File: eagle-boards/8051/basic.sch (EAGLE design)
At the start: 12 parts, among them IC1 AT89S51-24P, Q1 12M

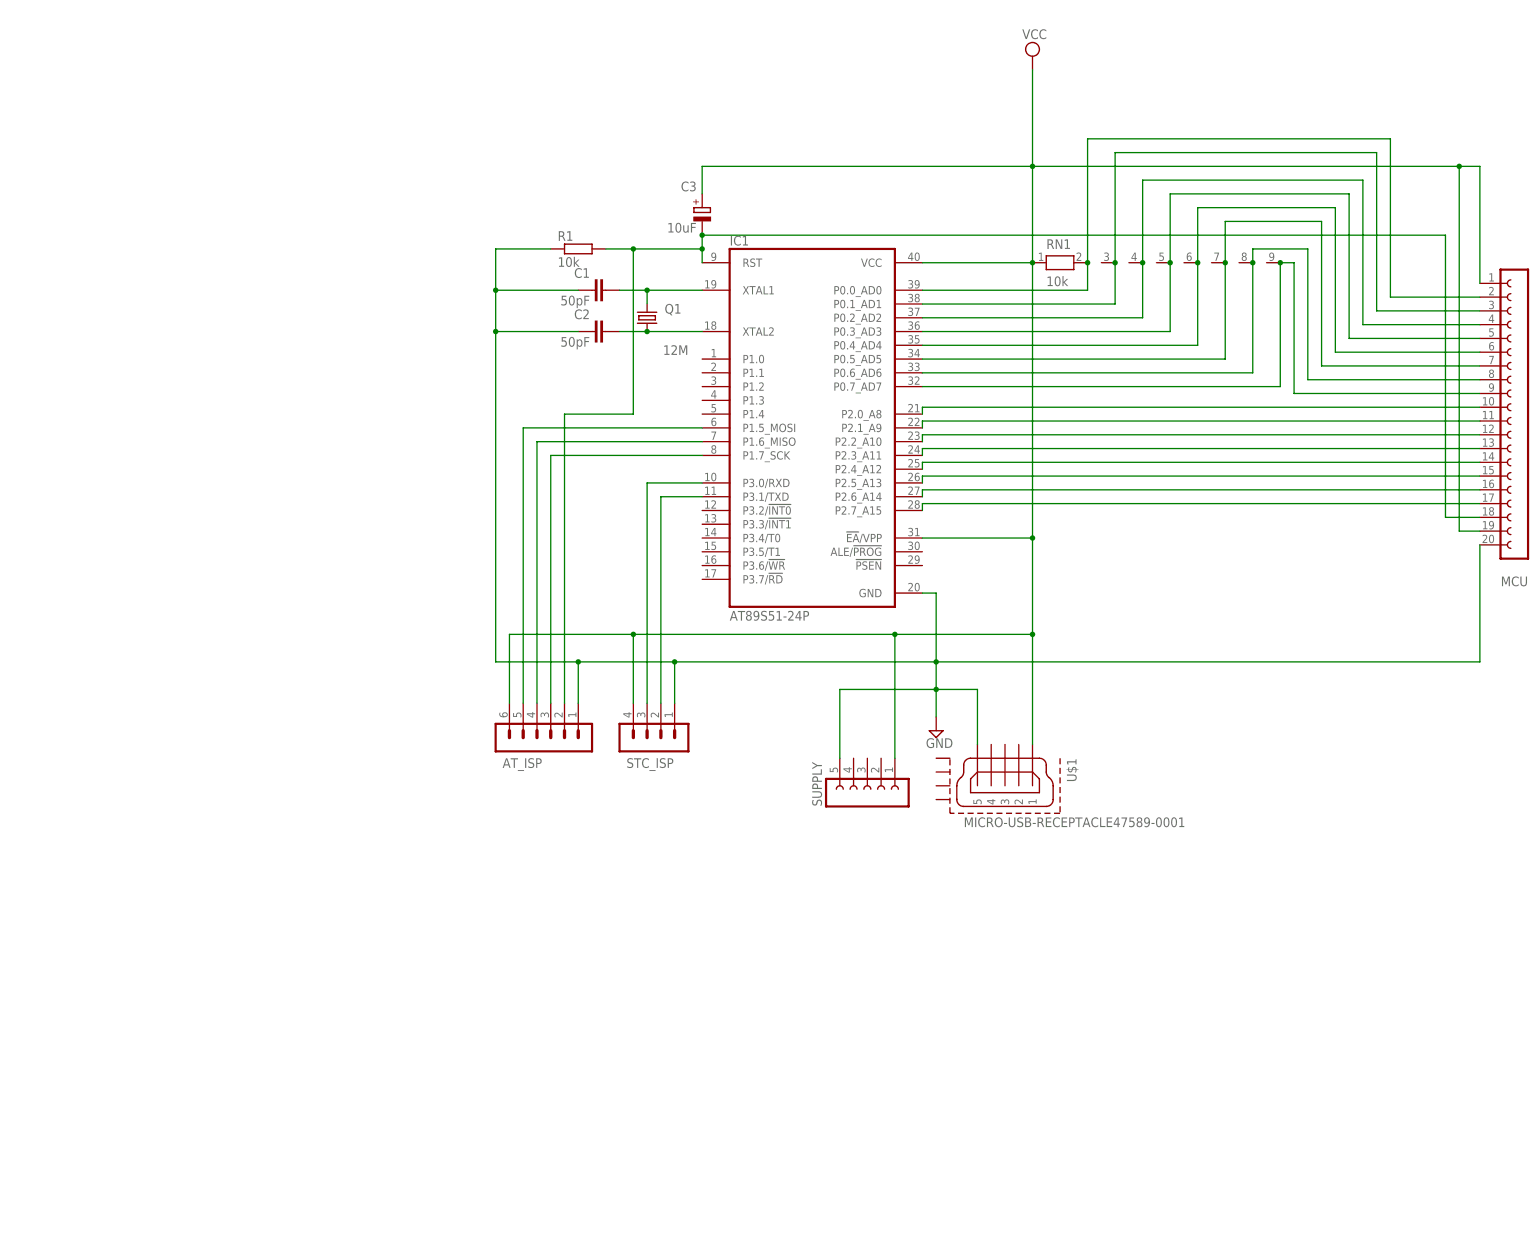
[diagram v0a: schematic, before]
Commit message: New revision for the STC89C52 controller board.
Include (optional) CP2104 USB-to-UART adapter to make it easier to program the board in-system.

Include a latching pushbutton for power, which is also needed to work correctly for in-system programming.
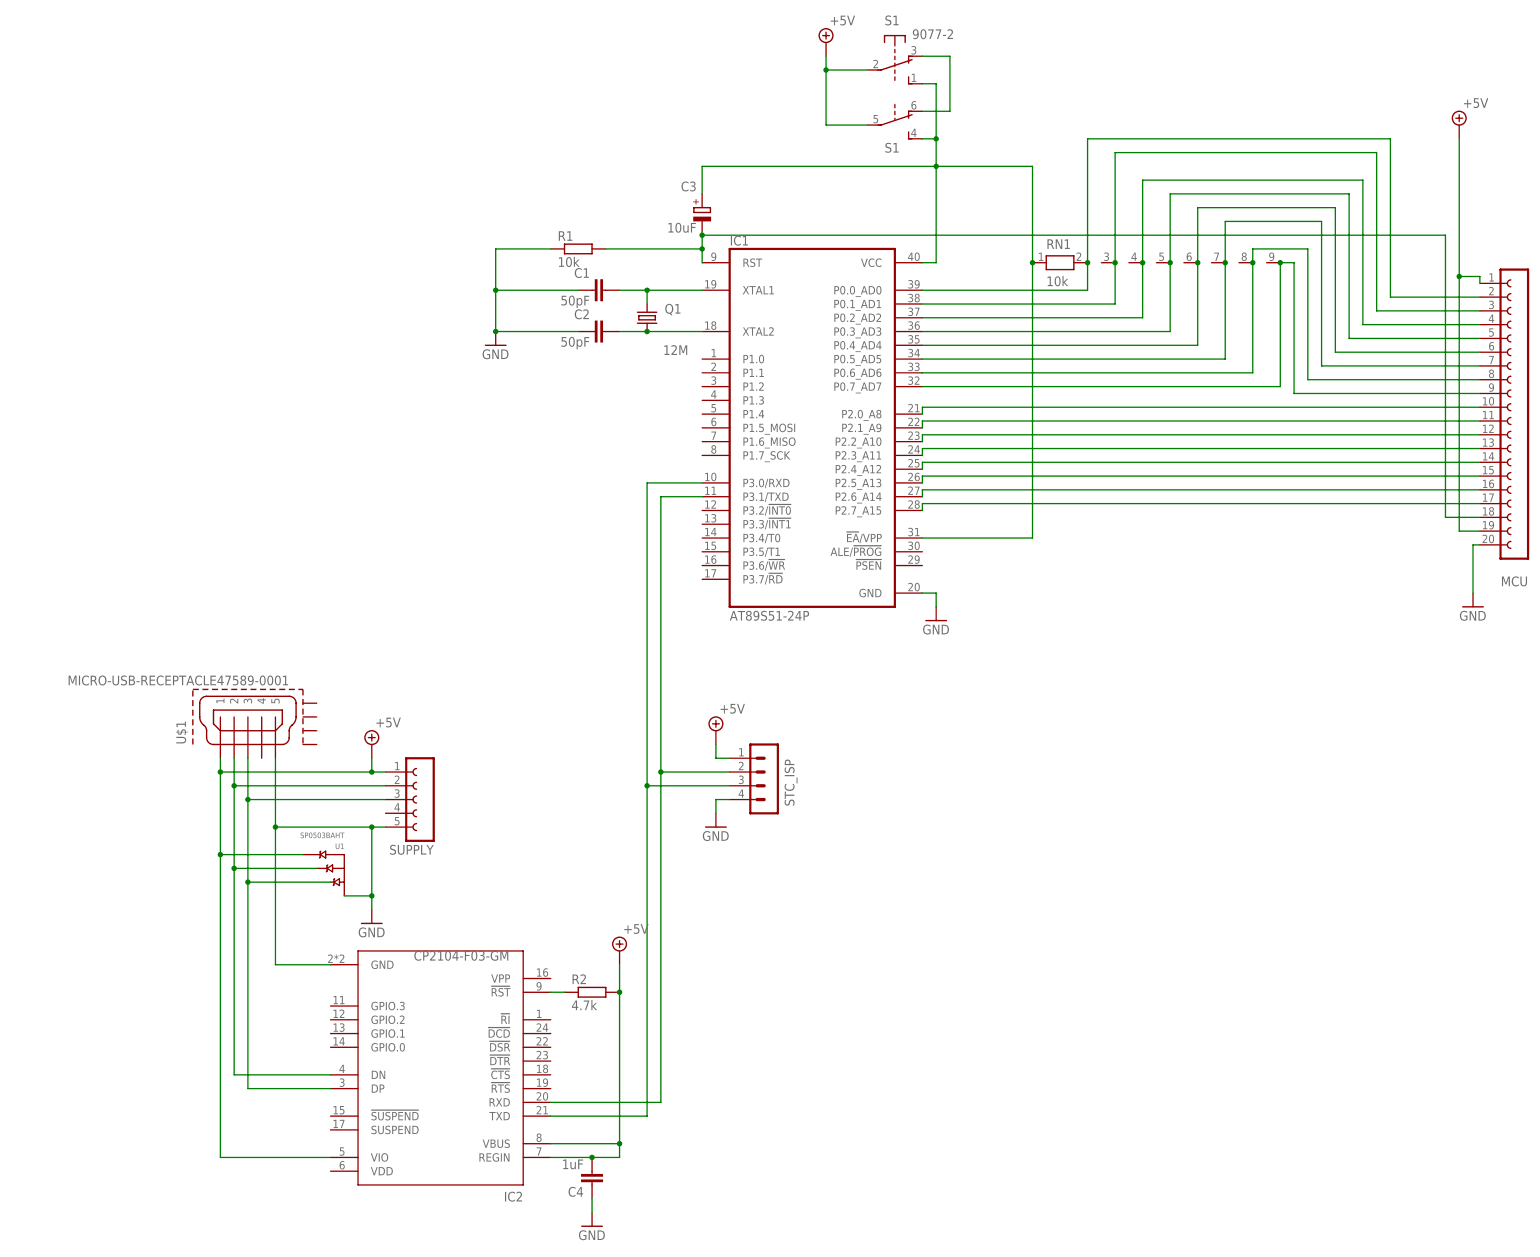
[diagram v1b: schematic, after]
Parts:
- removed AT_ISP: (no value), con-lstb:MA06-1
- added C4: 1uF, rcl:C-EU025-024X044
- added IC2: CP2104-F03-GM, CP2104:CP2104-F03-GM
- added R2: 4.7k, rcl:R-EU_0207/10
- added S1: 9077-2, switch-misc:9077-2
- added U1: SP0503BAHT, SP0503BAHT:SP0503BAHT
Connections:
- removed net N$49: AT_ISP.3, IC1.P1.7_SCK
- removed net N$50: AT_ISP.4, IC1.P1.6_MISO
- removed net N$51: AT_ISP.5, IC1.P1.5_MOSI
- removed net VCC: AT_ISP.6, C3.+, IC1.!EA!/VPP, IC1.VCC, MCU.1, MCU.19, RN1.1, STC_ISP.4, SUPPLY.1, U$1.1
- new net +5V: C4.2, IC2.REGIN, IC2.VBUS, IC2.VIO, MCU.1, MCU.19, R2.2, S11.P, S12.P, STC_ISP.1, SUPPLY.1, U$1.1, U1.C
- new net N$1: IC2.DN, SUPPLY.2, U$1.2, U1.B
- new net N$20: IC2.DP, SUPPLY.3, U$1.3, U1.A
- new net N$23: S11.O, S12.O
- new net N$24: IC2.!RST!, R2.1
- new net N$27: C3.+, IC1.!EA!/VPP, IC1.VCC, RN1.1, S11.S, S12.S
- net GND: now also C4.1, IC2.GND, STC_ISP.4, U1.GND; no longer AT_ISP.1, STC_ISP.1
- net N$18: now also IC2.TXD
- net N$5: no longer AT_ISP.2
- net N$52: now also IC2.RXD
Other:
- moved on the sheet: STC_ISP, SUPPLY, U$1

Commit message: Update components and layout for 8051 board.
Replace the microUSB connector to be the same Amphenol part as used in the ATmega board.

Replace the single electrolytic with a ceramic capacitor, and match the footprint between that and the CP2104 one.
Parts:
- C3: device rcl:CPOL-EUE2.5-6 -> capacitor-wima:C2.5/2
- C4: device rcl:C-EU025-024X044 -> capacitor-wima:C2.5/2
- U$1: value MICRO-USB-RECEPTACLE47589-0001 -> 10103594-0001LF; device con-molex-usb:MICRO-USB-RECEPTACLE47589-0001 -> 10103594-0001LF:10103594-0001LF
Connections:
- net N$27: now also C3.1; no longer C3.+
- net N$5: now also C3.2; no longer C3.-
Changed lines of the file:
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@@
 <part name="C1" library="rcl" library_urn="urn:adsk.eagle:library:334" deviceset="C-EU" device="050-025X075" package3d_urn="urn:adsk.eagle:package:23637/1" value="50pF"/>
 <part name="C2" library="rcl" library_urn="urn:adsk.eagle:library:334" deviceset="C-EU" device="050-025X075" package3d_urn="urn:adsk.eagle:package:23637/1" value="50pF"/>
-<part name="C3" library="rcl" library_urn="urn:adsk.eagle:library:334" deviceset="CPOL-EU" device="E2.5-6" package3d_urn="urn:adsk.eagle:package:23349/1" value="10uF"/>
+<part name="C3" library="capacitor-wima" library_urn="urn:adsk.eagle:library:116" deviceset="C" device="2.5/2" package3d_urn="urn:adsk.eagle:package:5415/1" value="10uF"/>
 <part name="R1" library="rcl" library_urn="urn:adsk.eagle:library:334" deviceset="R-EU_" device="0207/10" package3d_urn="urn:adsk.eagle:package:23491/2" value="10k"/>
-<part name="U$1" library="con-molex-usb" deviceset="MICRO-USB-RECEPTACLE" device="47589-0001"/>
+<part name="U$1" library="10103594-0001LF" deviceset="10103594-0001LF" device=""/>
 <part name="STC_ISP" library="con-lstb" library_urn="urn:adsk.eagle:library:162" deviceset="MA04-1" device="" package3d_urn="urn:adsk.eagle:package:8337/1"/>
 <part name="MCU" library="con-lsta" library_urn="urn:adsk.eagle:library:161" deviceset="FE20-1" device="" package3d_urn="urn:adsk.eagle:package:8196/1"/>
@@
 <part name="GND2" library="supply1" library_urn="urn:adsk.eagle:library:371" deviceset="GND" device=""/>
 <part name="SUPPLY5" library="supply2" library_urn="urn:adsk.eagle:library:372" deviceset="+5V" device=""/>
-<part name="C4" library="rcl" library_urn="urn:adsk.eagle:library:334" deviceset="C-EU" device="025-024X044" package3d_urn="urn:adsk.eagle:package:23630/1" value="1uF"/>
+<part name="C4" library="capacitor-wima" library_urn="urn:adsk.eagle:library:116" deviceset="C" device="2.5/2" package3d_urn="urn:adsk.eagle:package:5415/1" value="1uF"/>
 <part name="GND3" library="supply1" library_urn="urn:adsk.eagle:library:371" deviceset="GND" device=""/>
 <part name="U1" library="SP0503BAHT" deviceset="SP0503BAHT" device=""/>
@@
 <attribute name="VALUE" x="21.59" y="72.898" size="1.778" layer="96"/>
 </instance>
-<instance part="U$1" gate="G$1" x="-35.56" y="-12.7" smashed="yes" rot="R90">
-<attribute name="NAME" x="-46.99" y="-15.24" size="1.778" layer="95" font="vector" rot="R90"/>
-<attribute name="VALUE" x="-27.94" y="-2.54" size="1.778" layer="96" font="vector" rot="R180"/>
+<instance part="U$1" gate="G$1" x="-33.02" y="-5.08" smashed="yes" rot="R90">
+<attribute name="NAME" x="-44.45" y="-7.62" size="1.778" layer="95" font="vector" rot="R90"/>
+<attribute name="VALUE" x="-25.4" y="5.08" size="1.778" layer="96" font="vector" rot="R180"/>
 </instance>
 <instance part="STC_ISP" gate="1" x="60.96" y="-22.86" smashed="yes" rot="R180">
@@
 <wire x1="-12.7" y1="-30.48" x2="-10.16" y2="-30.48" width="0.1524" layer="91"/>
 <pinref part="U$1" gate="G$1" pin="5"/>
-<wire x1="-30.48" y1="-17.78" x2="-30.48" y2="-30.48" width="0.1524" layer="91"/>
+<wire x1="-30.48" y1="-15.24" x2="-30.48" y2="-30.48" width="0.1524" layer="91"/>
 <wire x1="-30.48" y1="-30.48" x2="-12.7" y2="-30.48" width="0.1524" layer="91"/>
 <junction x="-12.7" y="-30.48"/>
@@
 <segment>
 <pinref part="IC1" gate="P" pin="RST"/>
-<pinref part="C3" gate="G$1" pin="-"/>
+<pinref part="C3" gate="G$1" pin="2"/>
 <wire x1="48.26" y1="78.74" x2="48.26" y2="76.2" width="0.1524" layer="91"/>
 <pinref part="R1" gate="G$1" pin="2"/>
@@
 <wire x1="-12.7" y1="-20.32" x2="-12.7" y2="-17.78" width="0.1524" layer="91"/>
 <pinref part="U$1" gate="G$1" pin="1"/>
-<wire x1="-40.64" y1="-17.78" x2="-40.64" y2="-20.32" width="0.1524" layer="91"/>
+<wire x1="-40.64" y1="-15.24" x2="-40.64" y2="-20.32" width="0.1524" layer="91"/>
 <wire x1="-40.64" y1="-20.32" x2="-12.7" y2="-20.32" width="0.1524" layer="91"/>
 <junction x="-12.7" y="-20.32"/>
@@
 <segment>
 <pinref part="U$1" gate="G$1" pin="2"/>
-<wire x1="-38.1" y1="-17.78" x2="-38.1" y2="-22.86" width="0.1524" layer="91"/>
+<wire x1="-38.1" y1="-15.24" x2="-38.1" y2="-22.86" width="0.1524" layer="91"/>
 <wire x1="-38.1" y1="-22.86" x2="-38.1" y2="-38.1" width="0.1524" layer="91"/>
 <pinref part="SUPPLY" gate="G$1" pin="2"/>
@@
 <pinref part="SUPPLY" gate="G$1" pin="3"/>
 <wire x1="-35.56" y1="-40.64" x2="-35.56" y2="-25.4" width="0.1524" layer="91"/>
-<wire x1="-35.56" y1="-25.4" x2="-35.56" y2="-17.78" width="0.1524" layer="91"/>
+<wire x1="-35.56" y1="-25.4" x2="-35.56" y2="-15.24" width="0.1524" layer="91"/>
 <wire x1="-10.16" y1="-25.4" x2="-35.56" y2="-25.4" width="0.1524" layer="91"/>
 <junction x="-35.56" y="-25.4"/>
@@
 <wire x1="88.9" y1="22.86" x2="109.22" y2="22.86" width="0.1524" layer="91"/>
 <pinref part="RN1" gate="1" pin="1"/>
-<pinref part="C3" gate="G$1" pin="+"/>
+<pinref part="C3" gate="G$1" pin="1"/>
 <wire x1="48.26" y1="86.36" x2="48.26" y2="91.44" width="0.1524" layer="91"/>
 <pinref part="S1" gate="1" pin="S"/>

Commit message: Replace the wima capacitor object with a generic one.
This is pretty much the same footprint (except the solder pad is slightly thinner), but it requires one less library, since the xtal's capacitors are coming from rcl as well.
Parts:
- C3, C4: device capacitor-wima:C2.5/2 -> rcl:C-EU025-025X050
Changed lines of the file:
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@@
 <part name="C1" library="rcl" library_urn="urn:adsk.eagle:library:334" deviceset="C-EU" device="050-025X075" package3d_urn="urn:adsk.eagle:package:23637/1" value="50pF"/>
 <part name="C2" library="rcl" library_urn="urn:adsk.eagle:library:334" deviceset="C-EU" device="050-025X075" package3d_urn="urn:adsk.eagle:package:23637/1" value="50pF"/>
-<part name="C3" library="capacitor-wima" library_urn="urn:adsk.eagle:library:116" deviceset="C" device="2.5/2" package3d_urn="urn:adsk.eagle:package:5415/1" value="10uF"/>
+<part name="C3" library="rcl" library_urn="urn:adsk.eagle:library:334" deviceset="C-EU" device="025-025X050" package3d_urn="urn:adsk.eagle:package:23629/2" value="10uF"/>
 <part name="R1" library="rcl" library_urn="urn:adsk.eagle:library:334" deviceset="R-EU_" device="0207/10" package3d_urn="urn:adsk.eagle:package:23491/2" value="10k"/>
 <part name="U$1" library="10103594-0001LF" deviceset="10103594-0001LF" device=""/>
@@
 <part name="GND2" library="supply1" library_urn="urn:adsk.eagle:library:371" deviceset="GND" device=""/>
 <part name="SUPPLY5" library="supply2" library_urn="urn:adsk.eagle:library:372" deviceset="+5V" device=""/>
-<part name="C4" library="capacitor-wima" library_urn="urn:adsk.eagle:library:116" deviceset="C" device="2.5/2" package3d_urn="urn:adsk.eagle:package:5415/1" value="1uF"/>
+<part name="C4" library="rcl" library_urn="urn:adsk.eagle:library:334" deviceset="C-EU" device="025-025X050" package3d_urn="urn:adsk.eagle:package:23629/2" value="1uF"/>
 <part name="GND3" library="supply1" library_urn="urn:adsk.eagle:library:371" deviceset="GND" device=""/>
 <part name="U1" library="SP0503BAHT" deviceset="SP0503BAHT" device=""/>
